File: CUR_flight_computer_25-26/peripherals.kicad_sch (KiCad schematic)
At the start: 17 parts, among them J13 Conn_01x04_Pin, Q1 NTR4003N, SW3 GSPTS0018, SW4 GSPTS0018, SW5 GSPTS0018

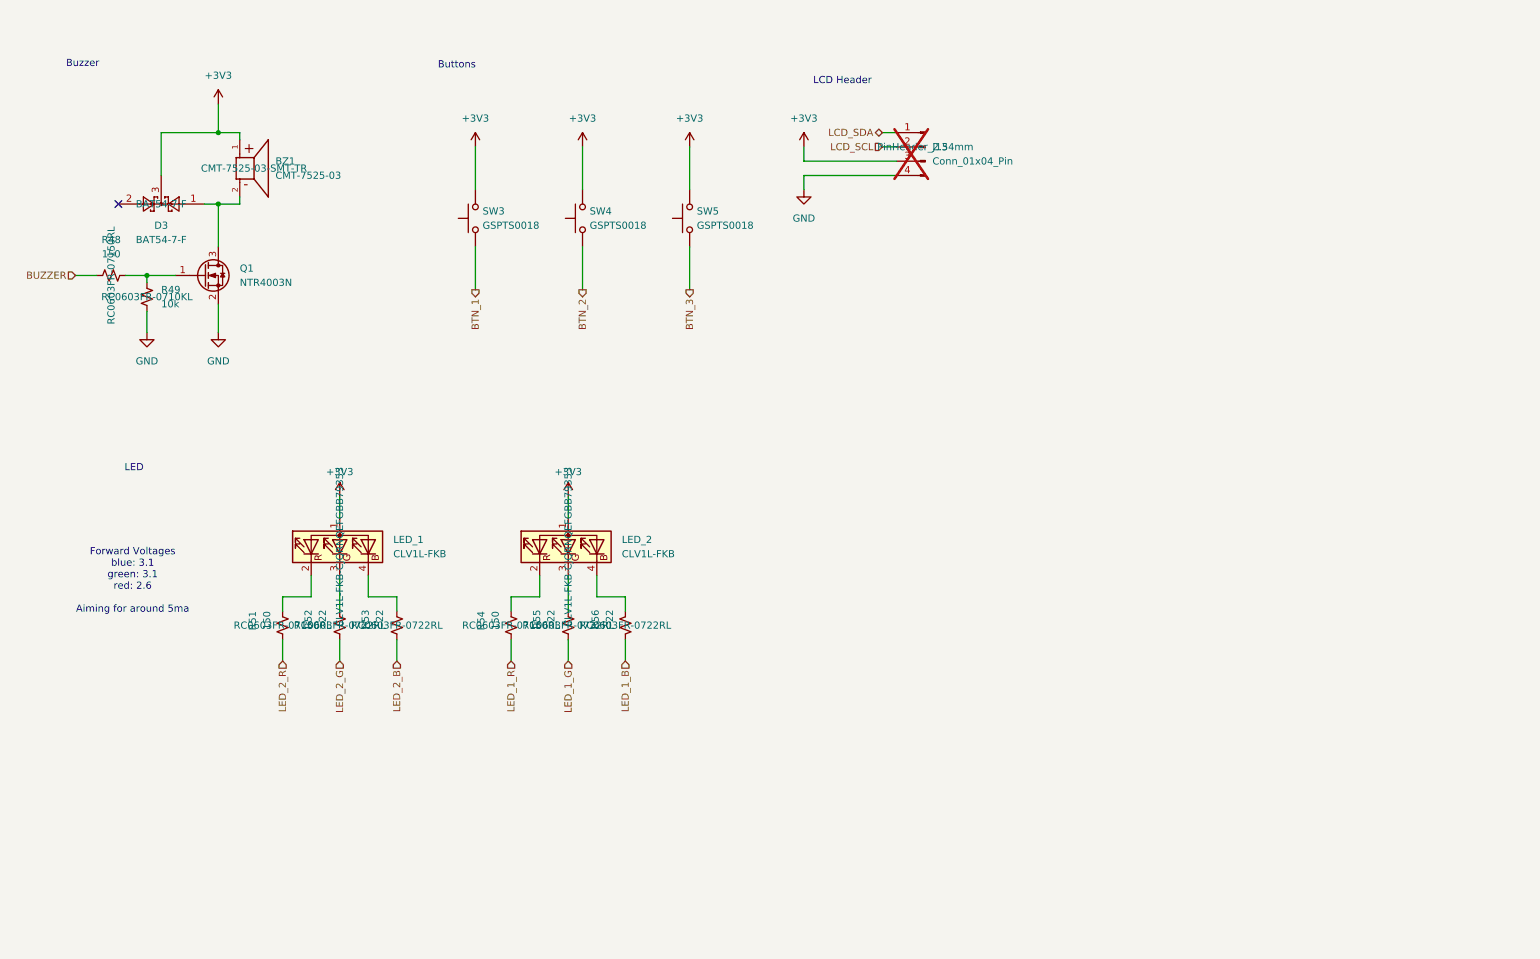
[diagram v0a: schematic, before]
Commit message: Hide MPNs
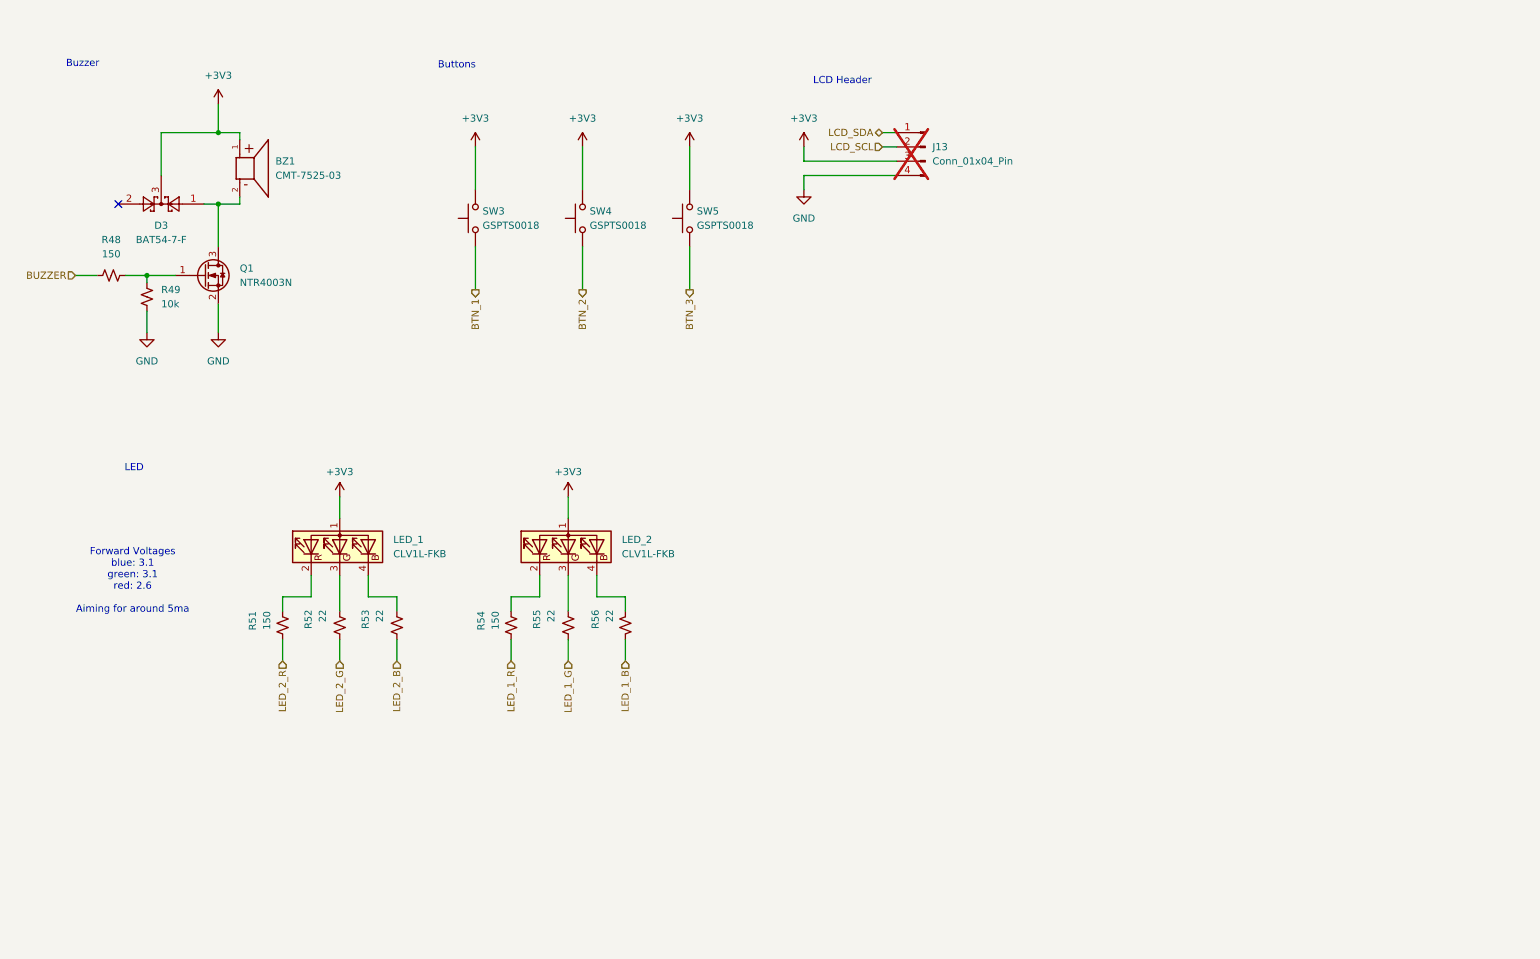
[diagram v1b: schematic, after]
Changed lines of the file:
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@@
 					(size 1.27 1.27)
 				)
+				(hide yes)
 			)
 		)
@@
 					(size 1.27 1.27)
 				)
+				(hide yes)
 			)
 		)
@@
 					(size 1.27 1.27)
 				)
+				(hide yes)
 			)
 		)
@@
 					(size 1.27 1.27)
 				)
+				(hide yes)
 			)
 		)
@@
 					(size 1.27 1.27)
 				)
+				(hide yes)
 			)
 		)
@@
 					(size 1.27 1.27)
 				)
+				(hide yes)
 			)
 		)
@@
 					(size 1.27 1.27)
 				)
+				(hide yes)
 			)
 		)
@@
 					(size 1.27 1.27)
 				)
+				(hide yes)
 			)
 		)
@@
 					(size 1.27 1.27)
 				)
+				(hide yes)
 			)
 		)
@@
 					(size 1.27 1.27)
 				)
+				(hide yes)
 			)
 		)
@@
 					(size 1.27 1.27)
 				)
+				(hide yes)
 			)
 		)
@@
 					(size 1.27 1.27)
 				)
+				(hide yes)
 			)
 		)
@@
 					(size 1.27 1.27)
 				)
-			)
-		)
+				(hide yes)
+			)
+		)

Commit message: Cleaned up schematic
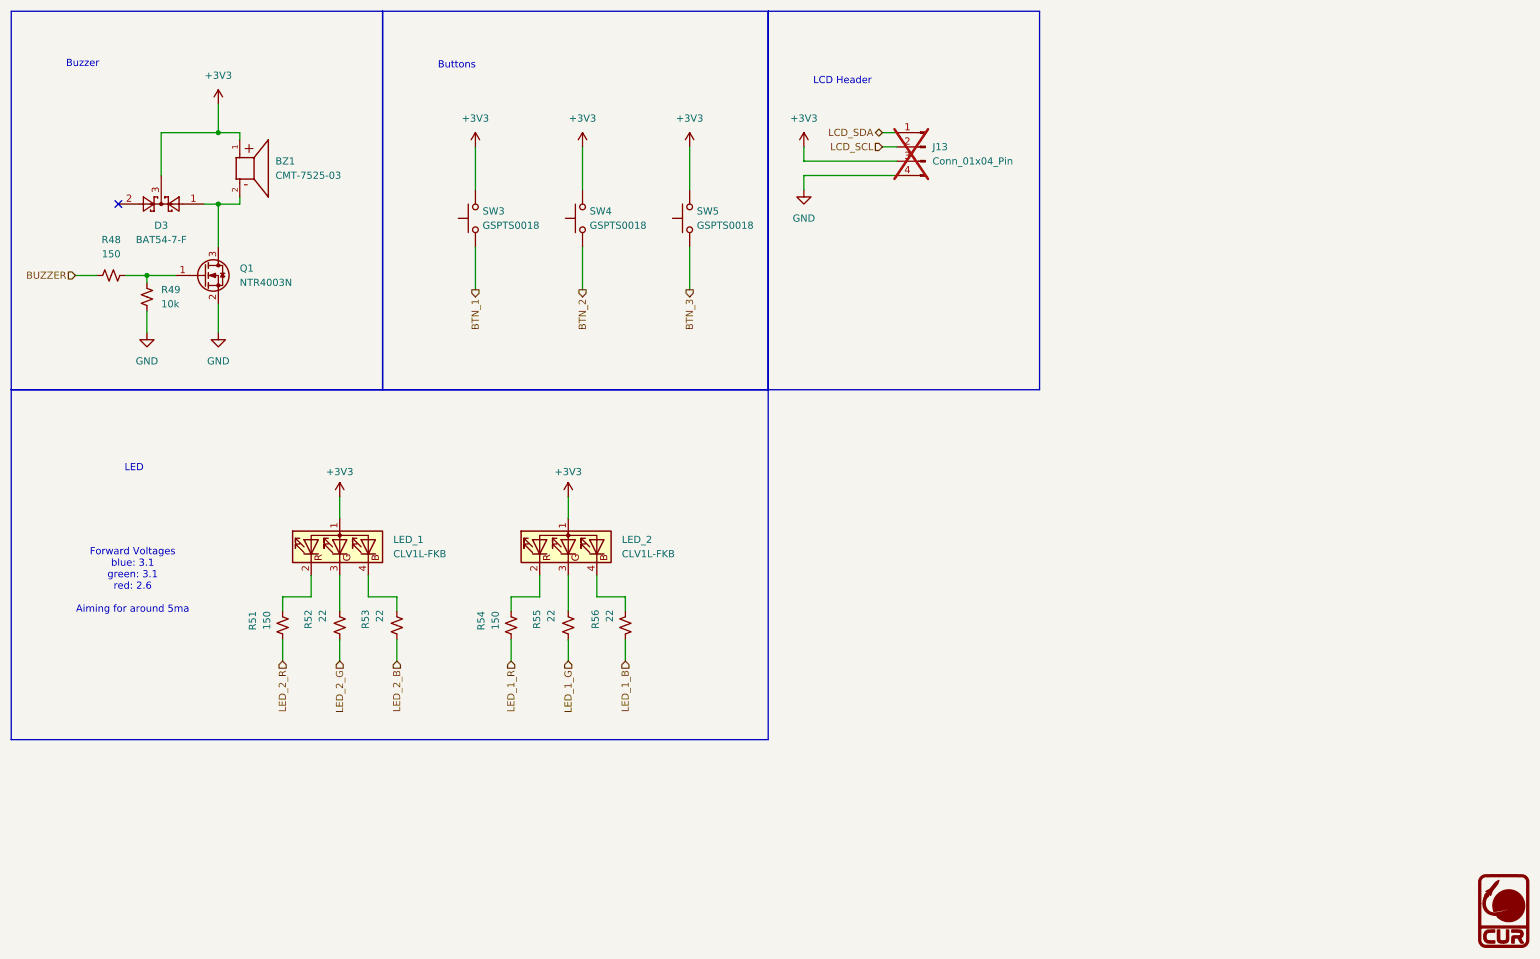
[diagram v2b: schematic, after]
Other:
- company: (none) -> Clarkson University Rocketry
- title: (none) -> Flight Computer
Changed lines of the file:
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@@
 	(generator_version "9.0")
 	(paper "A4")
+	(title_block
+		(title "Flight Computer")
+		(date "2026-03-18")
+		(company "Clarkson University Rocketry")
+	)
+	(rectangle
+		(start 13.97 81.28)
+		(end 148.59 143.51)
+		(stroke
+			(width 0)
+			(type default)
+		)
+		(fill
+			(type none)
+		)
+	)
+	(rectangle
+		(start 80.01 13.97)
+		(end 148.59 81.28)
+		(stroke
+			(width 0)
+			(type default)
+		)
+		(fill
+			(type none)
+		)
+	)
+	(rectangle
+		(start 148.59 13.97)
+		(end 196.85 81.28)
+		(stroke
+			(width 0)
+			(type default)
+		)
+		(fill
+			(type none)
+		)
+	)
+	(rectangle
+		(start 13.97 13.97)
+		(end 80.01 81.28)
+		(stroke
+			(width 0)
+			(type default)
+		)
+		(fill
+			(type none)
+		)
+	)
 	(text "LCD Header\n\n"
 		(exclude_from_sim no)
@@
 					(unit 1)
 				)
+			)
+		)
+	)
+	(symbol
+		(lib_id "CUR_Logo:LOGO")
+		(at 279.4 173.99 0)
+		(unit 1)
+		(exclude_from_sim no)
+		(in_bom yes)
+		(on_board yes)
+		(dnp no)
+		(fields_autoplaced yes)
+		(property "Reference" "#G11"
+			(at 279.4 167.002 0)
+			(effects
+				(font
+					(size 1.27 1.27)
+				)
+				(hide yes)
+			)
+		)
+		(property "Value" "LOGO"
+			(at 279.4 180.978 0)
+			(effects
+				(font
+					(size 1.27 1.27)
+				)
+				(hide yes)
+			)
+		)
+		(property "Footprint" ""
+			(at 279.4 173.99 0)
+			(effects
+				(font
+					(size 1.27 1.27)
+				)
+				(hide yes)
+			)
+		)
+		(property "Datasheet" ""
+			(at 279.4 173.99 0)
+			(effects
+				(font
+					(size 1.27 1.27)
+				)
+				(hide yes)
+			)
+		)
+		(property "Description" ""
+			(at 279.4 173.99 0)
+			(effects
+				(font
+					(size 1.27 1.27)
+				)
+				(hide yes)
+			)
+		)
+		(instances
+			(project "CUR_flight_computer_25-26"
+				(path "/bf7761cc-1b32-4d86-809c-5f027005229b/5946e354-b9a7-4a8a-8580-991442920c21"
+					(reference "#G11")
+					(unit 1)
+				)

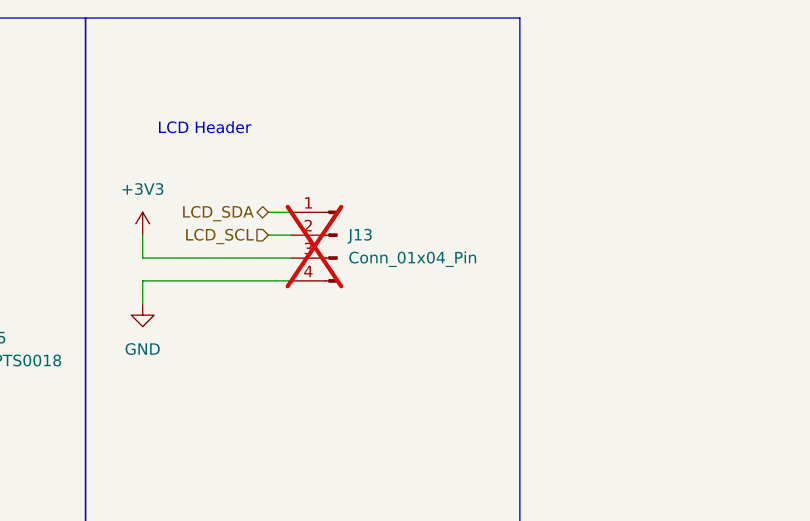
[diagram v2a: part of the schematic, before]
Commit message: Reroute flash and I2C
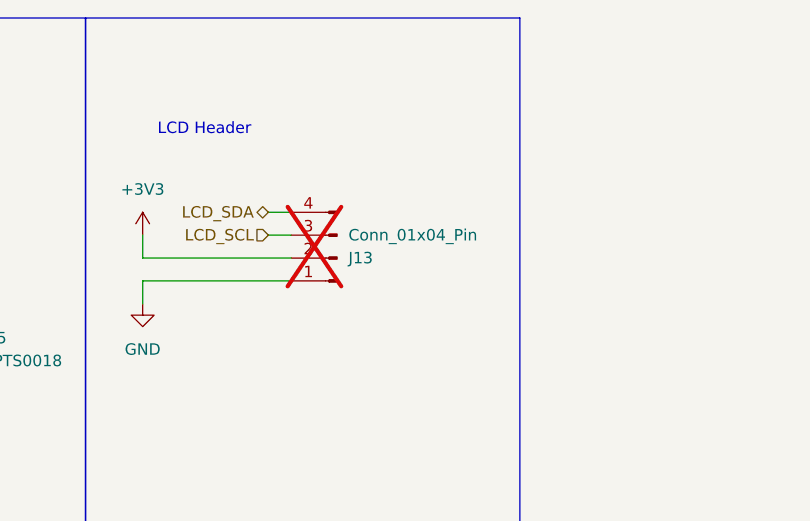
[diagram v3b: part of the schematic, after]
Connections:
- net +3V3: now also J13.2 (Pin_2); no longer J13.3 (Pin_3)
- net GND: now also J13.1 (Pin_1); no longer J13.4 (Pin_4)
- net LCD_SCL: now also J13.3 (Pin_3); no longer J13.2 (Pin_2)
- net LCD_SDA: now also J13.4 (Pin_4); no longer J13.1 (Pin_1)
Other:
- moved on the sheet: J13
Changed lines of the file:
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@@
 	(symbol
 		(lib_id "Connector:Conn_01x04_Pin")
-		(at 176.53 38.1 0)
-		(mirror y)
+		(at 176.53 40.64 180)
 		(unit 1)
 		(exclude_from_sim no)
@@
 		(on_board yes)
 		(dnp yes)
-		(fields_autoplaced yes)
 		(property "Reference" "J13"
-			(at 177.8 38.0999 0)
+			(at 177.8 40.6401 0)
 			(effects
 				(font
@@
 		)
 		(property "Value" "Conn_01x04_Pin"
-			(at 177.8 40.6399 0)
+			(at 177.8 38.1001 0)
 			(effects
 				(font
@@
 		)
 		(property "Footprint" "Connector_PinHeader_2.54mm:PinHeader_1x04_P2.54mm_Vertical"
-			(at 176.53 38.1 0)
+			(at 176.53 40.64 0)
 			(effects
 				(font
@@
 		)
 		(property "Datasheet" "~"
-			(at 176.53 38.1 0)
+			(at 176.53 40.64 0)
 			(effects
 				(font
@@
 		)
 		(property "Description" "Generic connector, single row, 01x04, script generated"
-			(at 176.53 38.1 0)
+			(at 176.53 40.64 0)
 			(effects
 				(font
@@
 		)
 		(property "MPN" "PinHeader_2.54mm"
-			(at 176.53 38.1 0)
+			(at 176.53 40.64 0)
 			(effects
 				(font

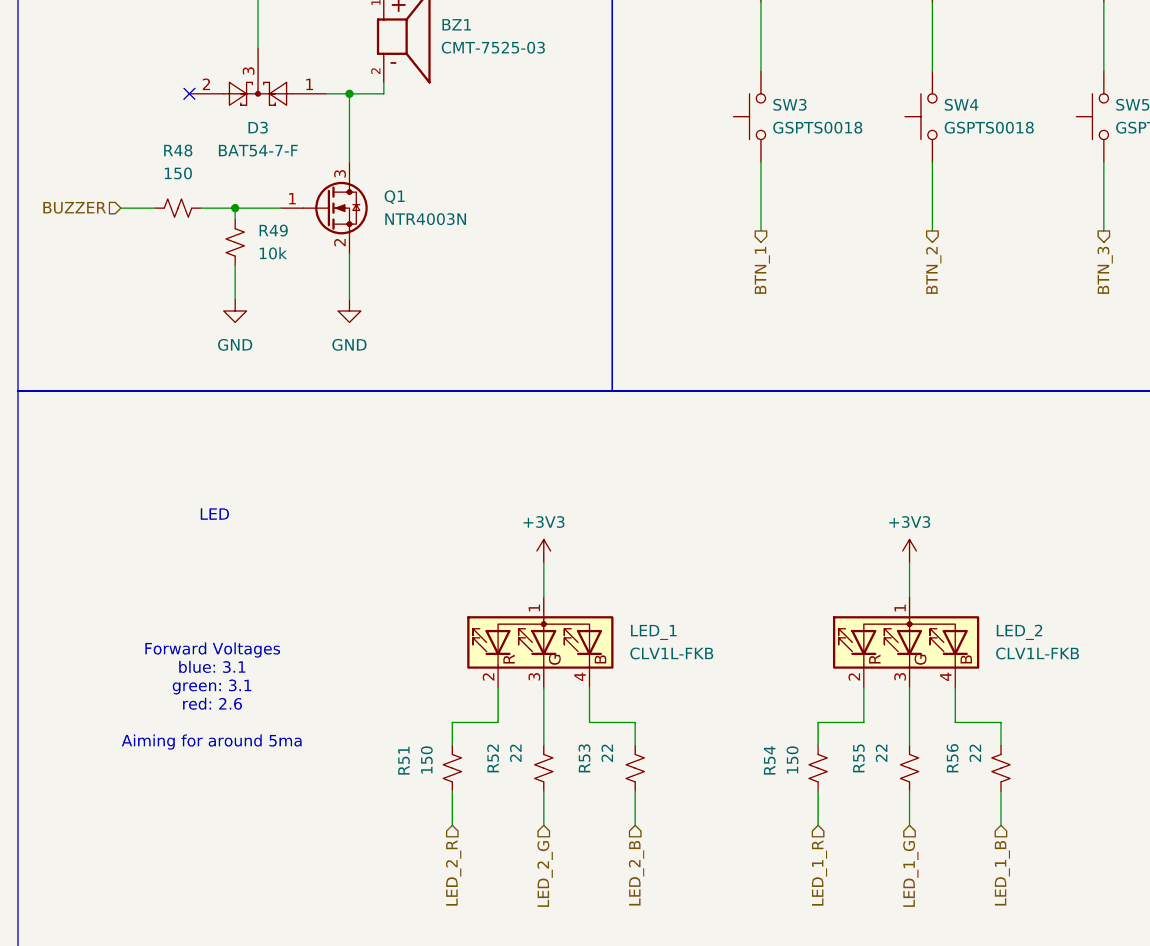
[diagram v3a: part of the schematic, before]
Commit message: BOM optimize resistors
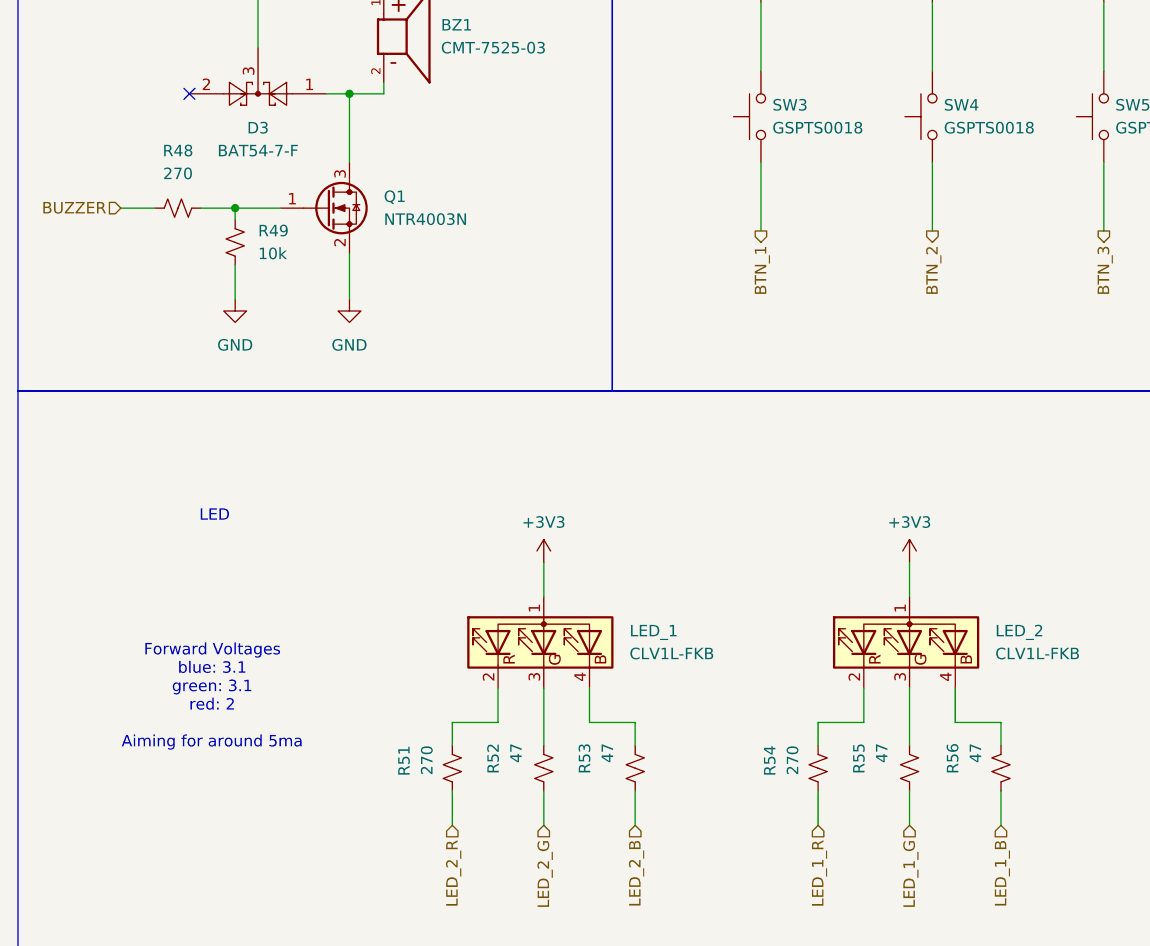
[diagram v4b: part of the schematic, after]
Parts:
- R48, R51, R54: value 150 -> 270
- R52, R53, R55, R56: value 22 -> 47
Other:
- note added: "Forward Voltages blue: 3.1 green: 3.1 red: 2 Aiming for around 5ma"
- note removed: "Forward Voltages blue: 3.1 green: 3.1 red: 2.6 Aiming for around 5ma"
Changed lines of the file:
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@@
 		)
 	)
-	(text "Forward Voltages\nblue: 3.1\ngreen: 3.1\nred: 2.6\n\nAiming for around 5ma\n"
+	(text "Forward Voltages\nblue: 3.1\ngreen: 3.1\nred: 2\n\nAiming for around 5ma\n"
 		(exclude_from_sim no)
 		(at 35.56 115.316 0)
@@
 			)
 		)
-		(property "Value" "22"
+		(property "Value" "47"
 			(at 69.342 120.396 90)
 			(effects
@@
 			)
 		)
-		(property "Value" "150"
+		(property "Value" "270"
 			(at 59.436 120.65 90)
 			(effects
@@
 			)
 		)
-		(property "Value" "150"
+		(property "Value" "270"
 			(at 100.076 120.65 90)
 			(effects
@@
 			)
 		)
-		(property "Value" "22"
+		(property "Value" "47"
 			(at 109.982 120.396 90)
 			(effects
@@
 			)
 		)
-		(property "Value" "22"
+		(property "Value" "47"
 			(at 120.396 120.396 90)
 			(effects
@@
 			)
 		)
-		(property "Value" "22"
+		(property "Value" "47"
 			(at 79.502 120.396 90)
 			(effects
@@
 			)
 		)
-		(property "Value" "150"
+		(property "Value" "270"
 			(at 31.75 57.15 90)
 			(effects

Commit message: Apply resistor MPNs
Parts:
- R48, R51, R54: MPN RC0603FR-07150RL -> RC0603JR-07270RL
- R52, R53, R55, R56: MPN RC0603FR-0722RL -> RC0603FR-0747RL
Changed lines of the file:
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@@
 			)
 		)
-		(property "MPN" "RC0603FR-0722RL"
+		(property "MPN" "RC0603FR-0747RL"
 			(at 72.39 123.19 0)
 			(effects
@@
 			)
 		)
-		(property "MPN" "RC0603FR-07150RL"
+		(property "MPN" "RC0603JR-07270RL"
 			(at 62.23 123.19 0)
 			(effects
@@
 			)
 		)
-		(property "MPN" "RC0603FR-07150RL"
+		(property "MPN" "RC0603JR-07270RL"
 			(at 102.87 123.19 0)
 			(effects
@@
 			)
 		)
-		(property "MPN" "RC0603FR-0722RL"
+		(property "MPN" "RC0603FR-0747RL"
 			(at 113.03 123.19 0)
 			(effects
@@
 			)
 		)
-		(property "MPN" "RC0603FR-0722RL"
+		(property "MPN" "RC0603FR-0747RL"
 			(at 123.19 123.19 0)
 			(effects
@@
 			)
 		)
-		(property "MPN" "RC0603FR-0722RL"
+		(property "MPN" "RC0603FR-0747RL"
 			(at 82.55 123.19 0)
 			(effects
@@
 			)
 		)
-		(property "MPN" "RC0603FR-07150RL"
+		(property "MPN" "RC0603JR-07270RL"
 			(at 31.75 60.96 0)
 			(effects
